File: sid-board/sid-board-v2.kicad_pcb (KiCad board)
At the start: 2 copper layers, 45 parts, among them J3 5V OUT, J4 3.3V OUT, J5 SPI/INT, Q1 BSS138, Q2 BSS138, Q3 BSS138, Q4 BSS138, U1 SC16IS752IPW, U2 MCP1703A-3302_SOT223, U3 PCA82C250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

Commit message: Updated SPI layout and README.md
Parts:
- J3: value 5V OUT -> 5V
- J4: value 3.3V OUT -> 3.3V
- J5: value SPI/INT -> SPI+IRQ
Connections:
- J5 pad 1: Net-(J5-Pad1) -> CLK
- J5 pad 2: Net-(J5-Pad2) -> MISO
- J5 pad 3: Net-(J5-Pad3) -> MOSI
- J5 pad 4: Net-(J5-Pad4) -> CS
- U1 pad 10: Net-(J5-Pad1) -> CS
- U1 pad 11: Net-(J5-Pad2) -> MOSI
- U1 pad 12: Net-(J5-Pad3) -> MISO
- U1 pad 13: Net-(J5-Pad4) -> CLK

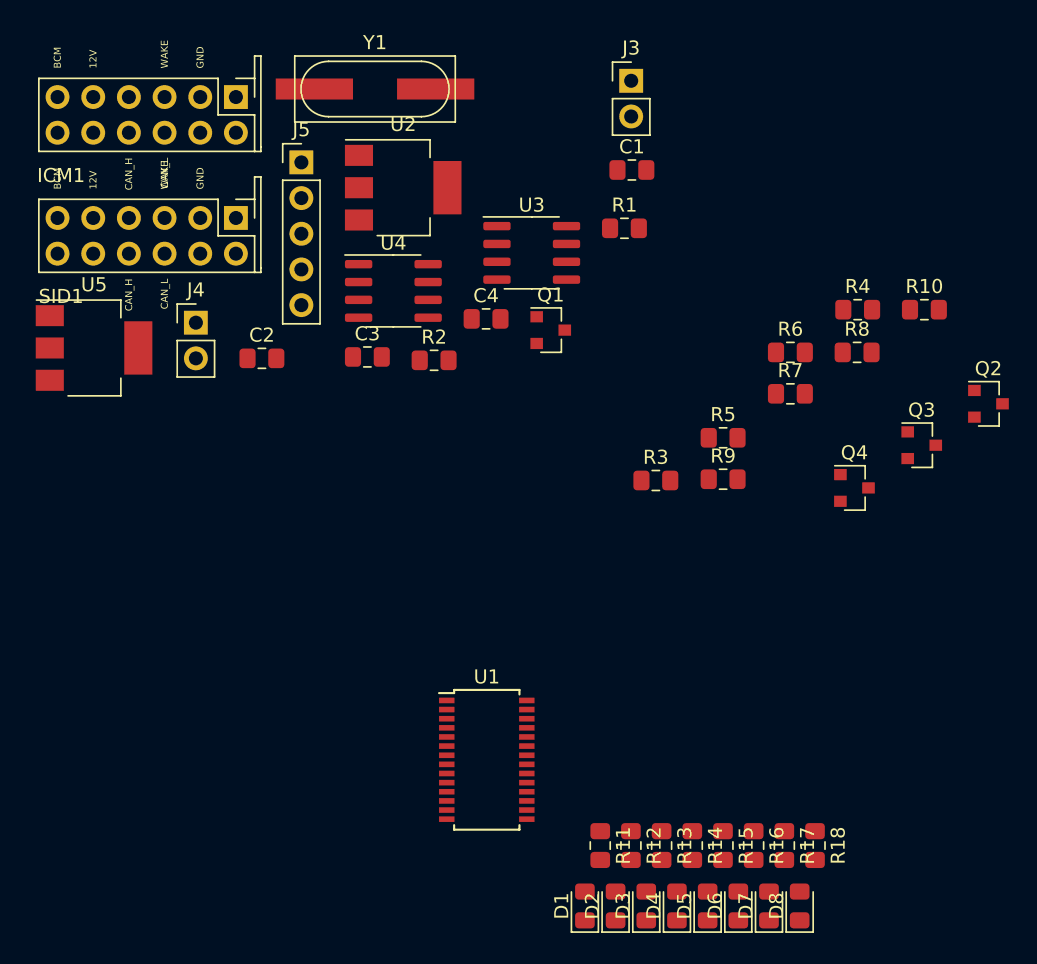
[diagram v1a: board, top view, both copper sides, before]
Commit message: Finished draft layout of sid-board v2
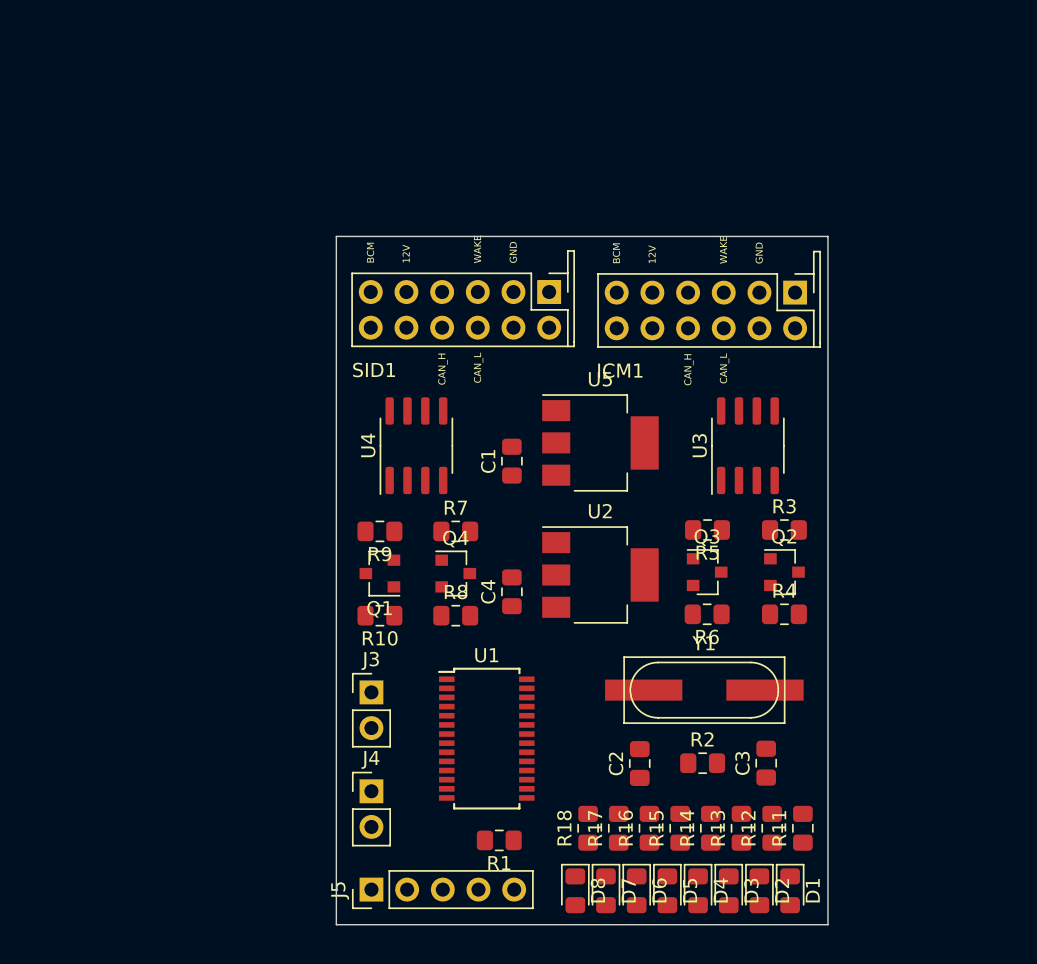
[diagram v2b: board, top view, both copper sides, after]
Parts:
- moved J5 52.0 mm to (84.5, 121.0), turned to 90 degrees
- moved Y1 48.8 mm to (108.2, 106.8)
- moved J3 47.3 mm to (84.5, 107.0)
- moved R1 44.5 mm to (93.6, 117.5), turned to 180 degrees
- moved R10 44.5 mm to (85.1, 101.5), turned to 180 degrees
- moved ICM1 42.2 mm to (108.3, 79.6)
- moved C3 40.5 mm to (112.6, 112.0), turned to 90 degrees
- moved C2 39.4 mm to (103.6, 112.0), turned to 90 degrees
- moved U5 36.7 mm to (100.8, 89.2)
- moved J4 35.6 mm to (84.5, 114.0)
- moved R2 34.5 mm to (108.1, 112.0)
- moved R8 34.2 mm to (90.5, 101.5)
- moved U2 30.9 mm to (100.8, 98.6)
- moved Q4 29.0 mm to (90.5, 98.5)
- moved R7 25.8 mm to (90.5, 95.5)
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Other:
- board outline added: 35 x 49 mm

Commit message: Working on routing of sidboard v2.
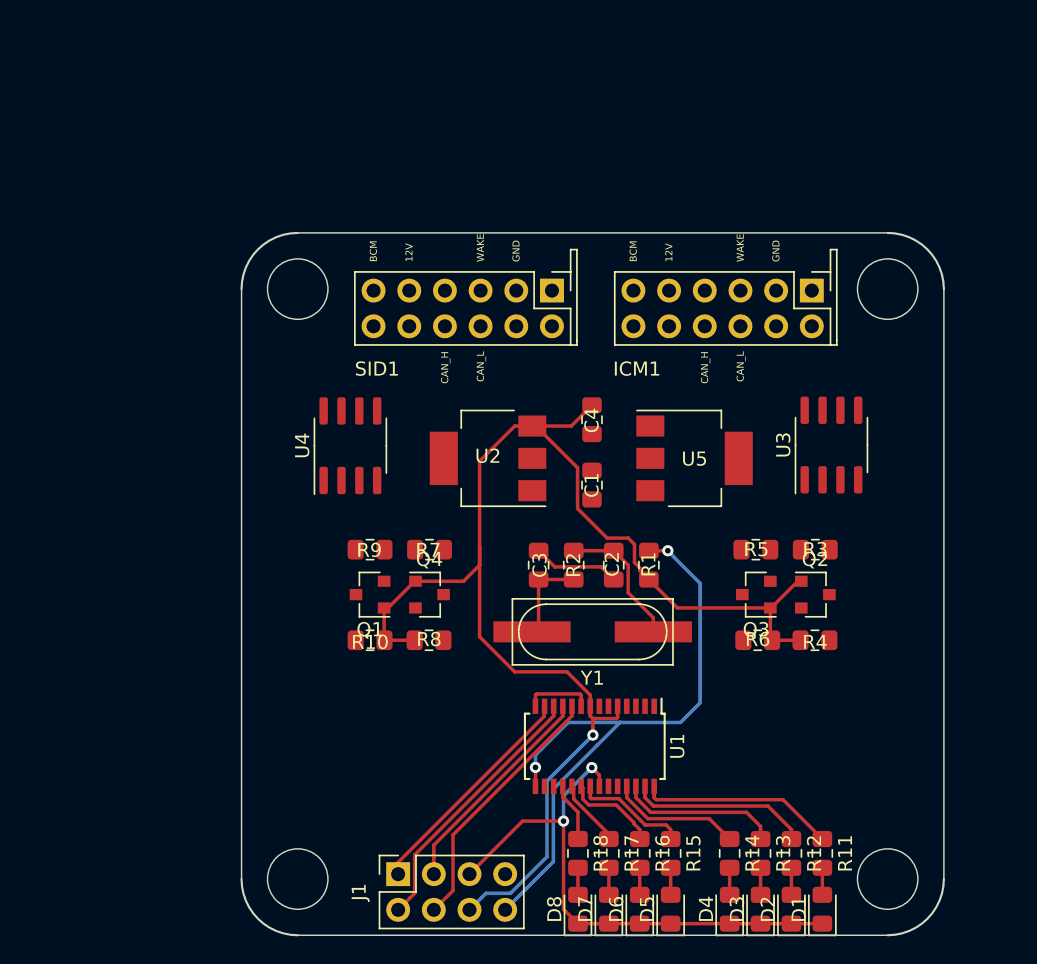
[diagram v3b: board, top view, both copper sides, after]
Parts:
- removed J3: 5V, Connector_PinHeader_2.54mm:PinHeader_1x02_P2.54mm_Vertical
- removed J4: 3.3V, Connector_PinHeader_2.54mm:PinHeader_1x02_P2.54mm_Vertical
- removed J5: SPI+IRQ, Connector_PinHeader_2.54mm:PinHeader_1x05_P2.54mm_Vertical
- added J1: SPI+IRQ+POWER, Connector_PinSocket_2.54mm:PinSocket_2x04_P2.54mm_Vertical, F.Cu at (86.4, 119.9)
- moved R1 22.3 mm to (104.2, 97.9), turned to 270 degrees
- moved C3 21.5 mm to (96.4, 97.9)
- moved R2 16.8 mm to (98.9, 97.9), turned to 90 degrees
- moved C2 14.2 mm to (101.8, 97.9), turned to 270 degrees
- moved C4 13.5 mm to (100.2, 87.5), turned to 270 degrees
- moved U2 11.5 mm to (92.8, 90.3), turned to 180 degrees
- moved Y1 8.97 mm to (100.2, 102.7), turned to 180 degrees
- moved U1 7.71 mm to (100.4, 110.8), turned to 270 degrees
- moved U5 6.79 mm to (107.5, 90.3)
- moved U3 5.95 mm to (117.2, 89.3)
- moved C1 5.95 mm to (100.2, 92.2)
- moved U4 4.70 mm to (83.0, 89.4)
- moved R6 4.05 mm to (112.0, 103.2)
- moved Q3 3.85 mm to (111.9, 100.0), turned to 180 degrees
- moved R5 3.72 mm to (111.9, 96.8)
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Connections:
- net Net-(J5-Pad5) renamed IRQ
- ICM1 pad 1: Net-(ICM1-Pad1) -> (no net)
- ICM1 pad 11: Net-(ICM1-Pad11) -> (no net)
- ICM1 pad 12: Net-(ICM1-Pad12) -> (no net)
- ICM1 pad 4: Net-(ICM1-Pad4) -> (no net)
- ICM1 pad 7: Net-(ICM1-Pad7) -> (no net)
- ICM1 pad 8: Net-(ICM1-Pad8) -> (no net)
- SID1 pad 1: Net-(SID1-Pad1) -> (no net)
- SID1 pad 11: Net-(SID1-Pad11) -> (no net)
- SID1 pad 12: Net-(SID1-Pad12) -> (no net)
- SID1 pad 4: Net-(SID1-Pad4) -> (no net)
- SID1 pad 7: Net-(SID1-Pad7) -> (no net)
- SID1 pad 8: Net-(SID1-Pad8) -> (no net)
- U1 pad 1: Net-(U1-Pad1) -> (no net)
- U1 pad 16: Net-(U1-Pad16) -> (no net)
- U1 pad 17: Net-(U1-Pad17) -> (no net)
- U1 pad 2: Net-(U1-Pad2) -> (no net)
- U3 pad 5: Net-(U3-Pad5) -> (no net)
- U4 pad 5: Net-(U4-Pad5) -> (no net)
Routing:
- net VDD_3.3V: track 0.00 -> 100.4 mm, vias 0 -> 1
- net GND: track 0.00 -> 50.7 mm, vias 0 -> 2
- net IRQ: track 0.00 -> 45.3 mm, vias 0 -> 2
- net MISO: track 0.00 -> 19.1 mm
- net CS: track 0.00 -> 18.6 mm
- net CLK: track 0.00 -> 16.3 mm
- net MOSI: track 0.00 -> 15.8 mm
- net Net-(R11-Pad1): track 0.00 -> 14.6 mm
- net Net-(R12-Pad1): track 0.00 -> 12.8 mm
- net Net-(R13-Pad1): track 0.00 -> 11.4 mm
- net XTAL2: track 0.00 -> 9.79 mm
- net Net-(R14-Pad1): track 0.00 -> 9.35 mm
- net Net-(R15-Pad1): track 0.00 -> 8.14 mm
- net Net-(R16-Pad1): track 0.00 -> 6.63 mm
- net XTAL1: track 0.00 -> 6.42 mm
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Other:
- board size 35 x 49 mm -> 50 x 50 mm

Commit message: Finished first draft PCB layout of SIDBOARD2
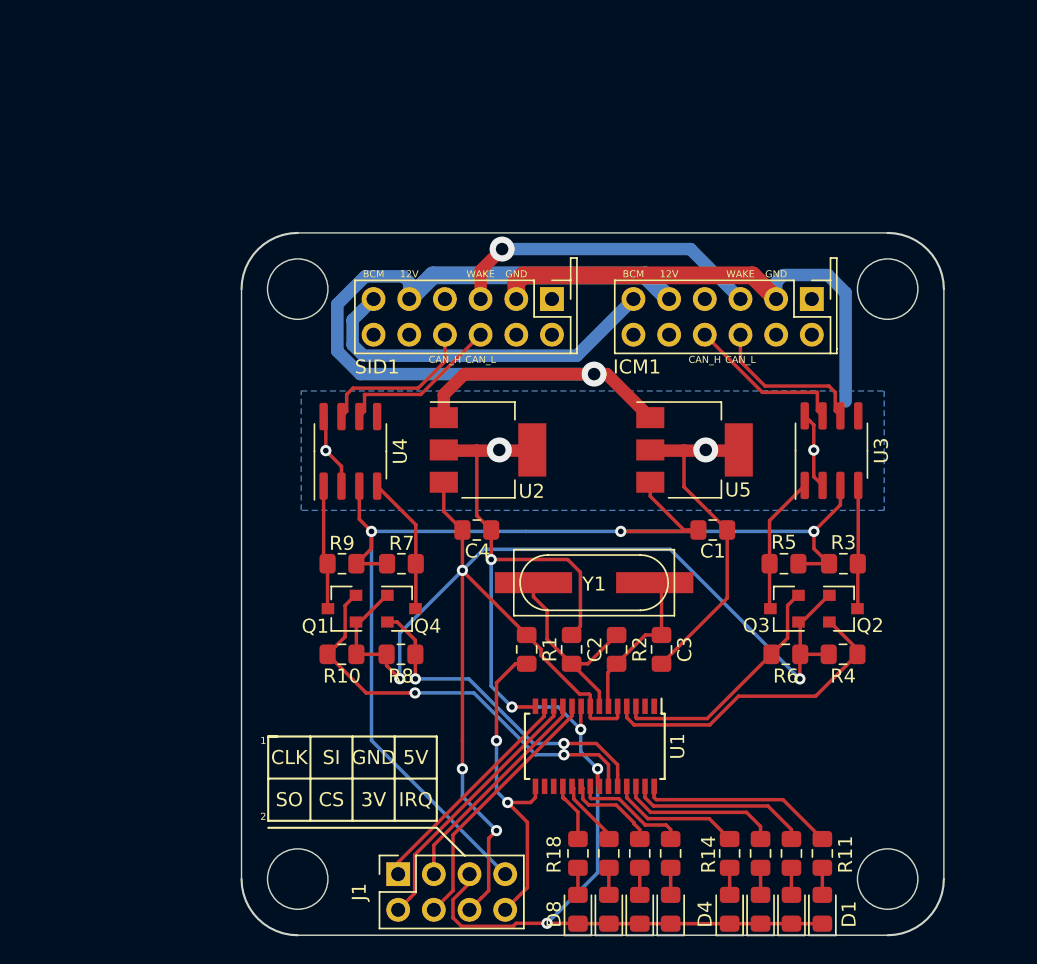
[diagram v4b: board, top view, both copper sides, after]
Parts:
- moved C4 11.4 mm to (92.0, 95.4), turned to 0 degrees
- moved C3 10.6 mm to (105.2, 103.9), turned to 270 degrees
- moved R1 10.6 mm to (95.5, 103.9), turned to 90 degrees
- moved C1 9.18 mm to (108.8, 95.4), turned to 0 degrees
- moved R2 6.73 mm to (102.0, 103.9)
- moved C2 6.71 mm to (98.8, 103.9), turned to 90 degrees
- moved Y1 3.50 mm to (100.3, 99.2), turned to 0 degrees
- moved Q1 2.24 mm to (82.4, 101.0)
- moved Q2 2.24 mm to (118.1, 101.0)
- moved Q3 2.24 mm to (113.9, 101.0)
- moved Q4 2.24 mm to (86.6, 101.0)
- moved R10 2.24 mm to (82.4, 104.2)
- moved R3 2.24 mm to (118.1, 97.8)
- moved R4 2.24 mm to (118.1, 104.2)
- moved R5 2.24 mm to (113.9, 97.8)
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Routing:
- net GND: track 50.7 -> 164.2 mm, vias 2 -> 9
- net VDD_5V: track 0.00 -> 88.3 mm, vias 0 -> 3
- net VIN: track 0.00 -> 67.7 mm, vias 0 -> 1
- net TXB: track 0.00 -> 29.9 mm, vias 0 -> 2
- net Net-(ICM1-Pad6): track 0.00 -> 25.9 mm
- net RXB: track 0.00 -> 23.8 mm, vias 0 -> 2
- net RXA: track 0.00 -> 22.7 mm
- net Net-(ICM1-Pad3): track 0.00 -> 22.6 mm, vias 0 -> 1
- net IRQ: track 45.3 -> 23.4 mm
- net TXA: track 0.00 -> 17.4 mm
- net Net-(SID1-Pad10): track 0.00 -> 11.8 mm
- net Net-(SID1-Pad9): track 0.00 -> 11.6 mm
- net Net-(ICM1-Pad9): track 0.00 -> 11.5 mm
- net Net-(ICM1-Pad10): track 0.00 -> 11.4 mm
- net RXB_CMOS: track 0.00 -> 9.88 mm
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- added copper zone on B.Cu, net GND
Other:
- board text added: "1"
- board text added: "2"
- board text added: "3V"
- board text added: "5V"
- board text added: "CLK"
- board text added: "CS"
- board text added: "GND"
- board text added: "IRQ"
- board text added: "SI"
- board text added: "SO"

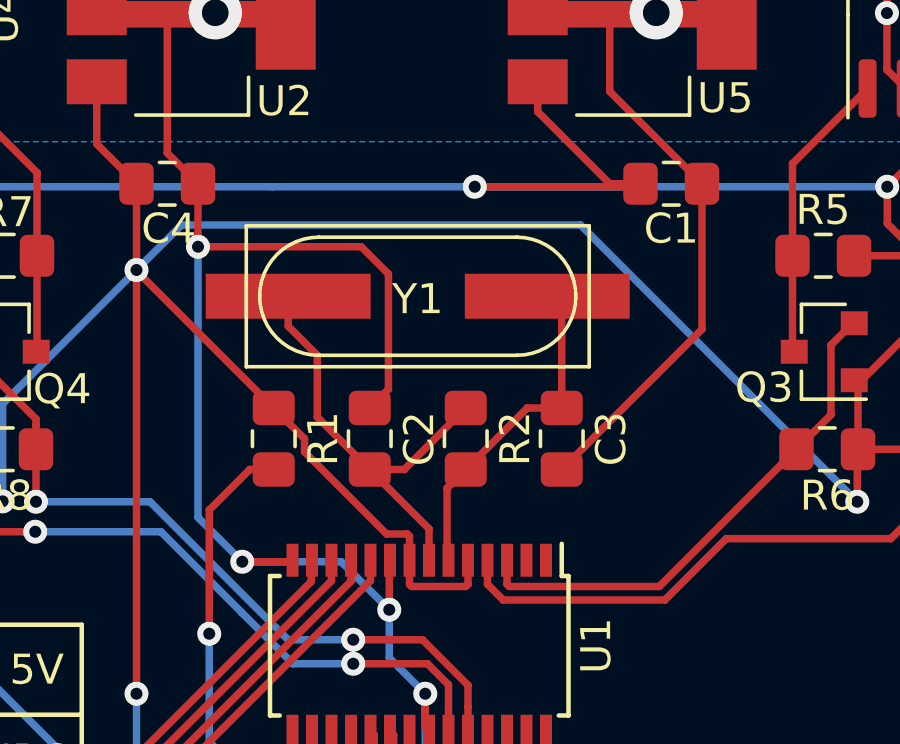
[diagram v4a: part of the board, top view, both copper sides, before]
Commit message: Replaced crystal with oscillator module on PCB
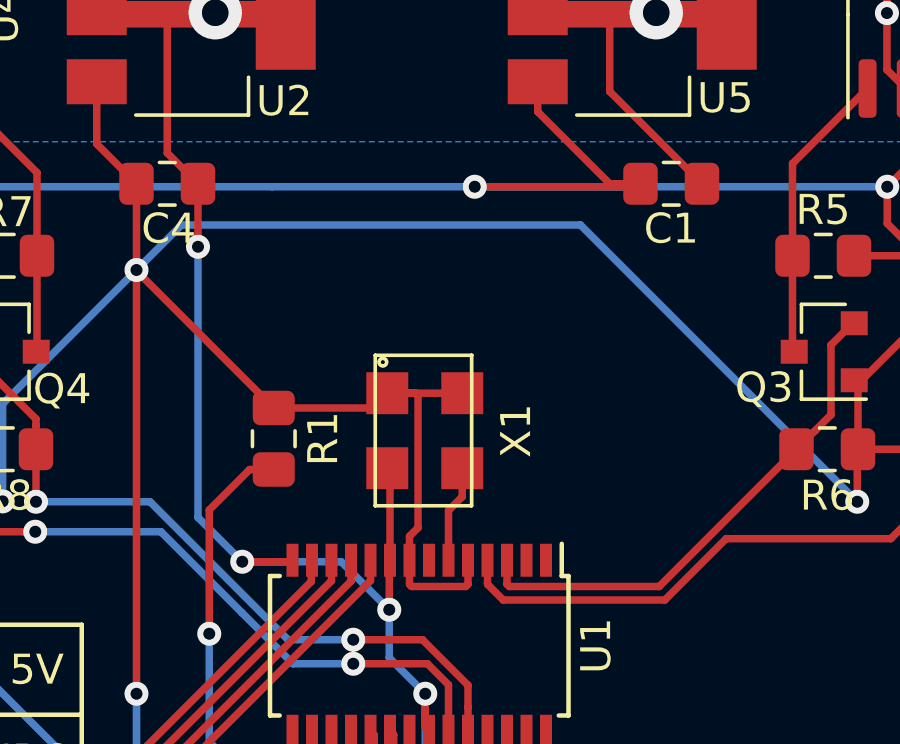
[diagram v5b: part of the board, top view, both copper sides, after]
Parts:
- removed C2, C3: 18pF, Capacitor_SMD:C_0805_2012Metric_Pad1.15x1.40mm_HandSolder
- removed R2: 1M, Resistor_SMD:R_0805_2012Metric_Pad1.15x1.40mm_HandSolder
- removed Y1: 14.7456MHz, sid-board:Euroquarts 14.7456MHz Crystal ±30ppm SMD 2-Pin 12.4 x 4.5 x 4.2mm
- added X1: S53305, sid-board:S53305-16.000-X, F.Cu at (100.6, 103.6)
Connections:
- ICM1 pad 1: (no net) -> Net-(ICM1-Pad1)
- ICM1 pad 11: (no net) -> Net-(ICM1-Pad11)
- ICM1 pad 12: (no net) -> Net-(ICM1-Pad12)
- ICM1 pad 4: (no net) -> Net-(ICM1-Pad4)
- ICM1 pad 7: (no net) -> Net-(ICM1-Pad7)
- ICM1 pad 8: (no net) -> Net-(ICM1-Pad8)
- SID1 pad 1: (no net) -> Net-(SID1-Pad1)
- SID1 pad 11: (no net) -> Net-(SID1-Pad11)
- SID1 pad 12: (no net) -> Net-(SID1-Pad12)
- SID1 pad 4: (no net) -> Net-(SID1-Pad4)
- SID1 pad 7: (no net) -> Net-(SID1-Pad7)
- SID1 pad 8: (no net) -> Net-(SID1-Pad8)
- U1 pad 1: (no net) -> Net-(U1-Pad1)
- U1 pad 16: (no net) -> Net-(U1-Pad16)
- U1 pad 17: (no net) -> Net-(U1-Pad17)
- U1 pad 2: (no net) -> Net-(U1-Pad2)
- U1 pad 7: XTAL2 -> Net-(U1-Pad7)
- U3 pad 5: (no net) -> Net-(U3-Pad5)
- U4 pad 5: (no net) -> Net-(U4-Pad5)
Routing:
- net GND: track 164.2 -> 144.4 mm
- net XTAL2: track 14.8 -> 0.00 mm
- net XTAL1: track 11.3 -> 3.26 mm
- net VDD_3.3V: track 107.0 -> 112.8 mm

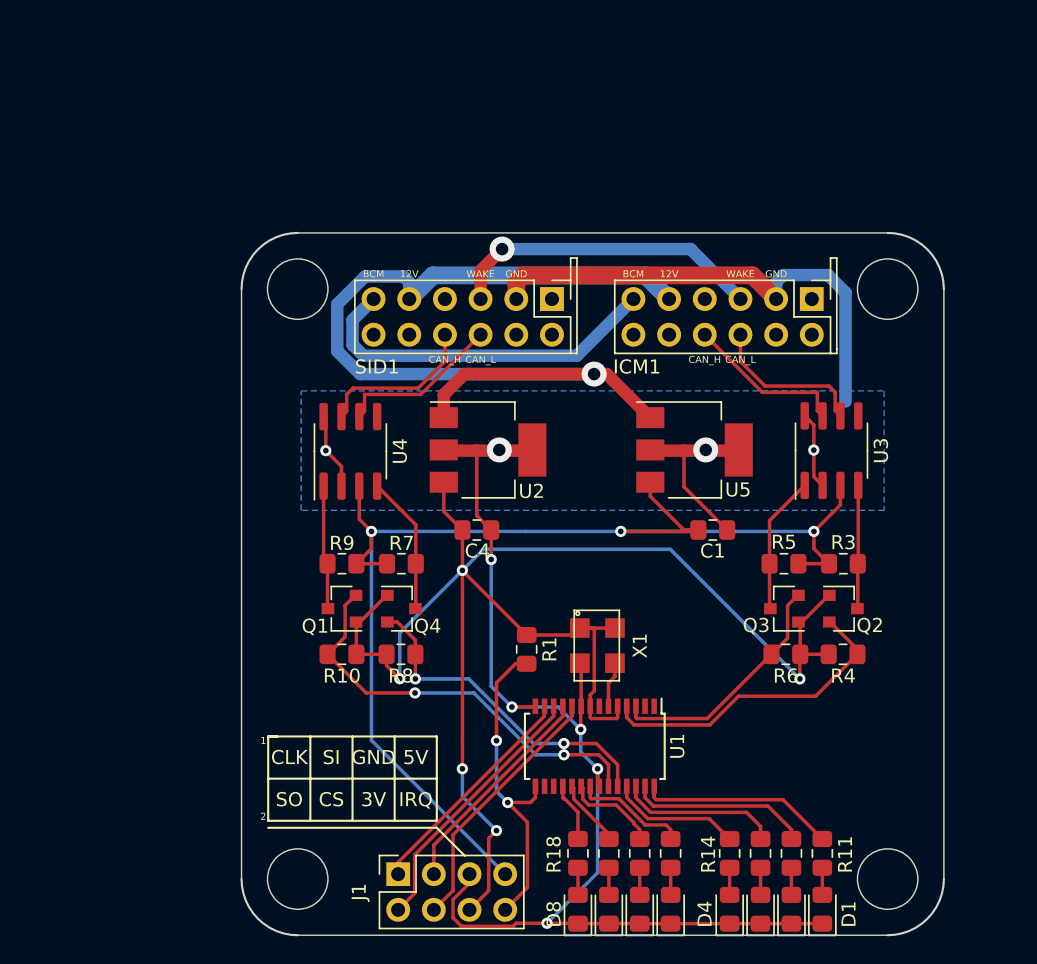
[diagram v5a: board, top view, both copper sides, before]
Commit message: Cleaned up v2 board for prototype production
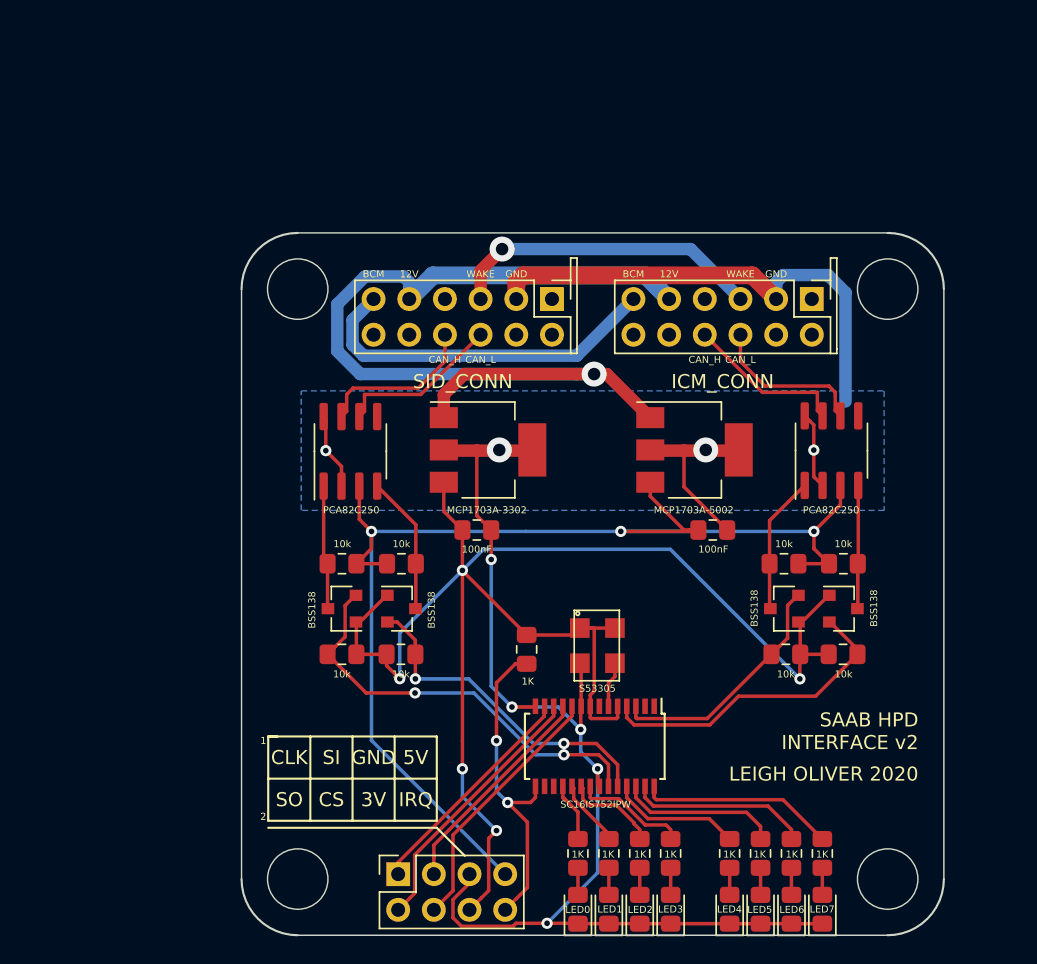
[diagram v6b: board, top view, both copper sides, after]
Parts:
- added G***: LOGO, sid-board:australia_map, B.Cu at (110.5, 111.8)
- U2: value MCP1703A-3302_SOT223 -> MCP1703A-3302
- U5: value MCP1703A-5002_SOT223 -> MCP1703A-5002
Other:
- board text added: "DESIGNED IN AUSTRALIA"
- board text added: "JLCJLCJLCJLC"
- board text added: "LEIGH OLIVER 2020"
- board text added: "SAAB HPD INTERFACE v2"
